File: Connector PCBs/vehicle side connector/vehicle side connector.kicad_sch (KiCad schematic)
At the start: 0 parts

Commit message: added connectors and pinout to schematics, imported board outline
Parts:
- added H? (x3): MountingHole_Pad, symbol Mechanical:MountingHole_Pad
- added J?: Conn_02x04_Odd_Even, symbol Connector_Generic:Conn_02x04_Odd_Even
- added J?: Conn_02x16_Odd_Even, symbol Connector_Generic:Conn_02x16_Odd_Even
- added J?: Conn_02x11_Odd_Even, symbol Connector_Generic:Conn_02x11_Odd_Even
- added J?: Conn_02x10_Odd_Even, symbol Connector_Generic:Conn_02x10_Odd_Even
- added R?: R, symbol Device:R
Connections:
- new net 5V: J?.14 (Pin_14), J?.16 (Pin_16), J?.21 (Pin_21), J?.22 (Pin_22)
- new net 5V_IN: J?.17 (Pin_17)
- new net CAN_H: J?.13 (Pin_13), J?.2 (Pin_2), J?.2 (Pin_2)
- new net CAN_L: J?.15 (Pin_15), J?.4 (Pin_4), J?.4 (Pin_4)
- new net CAPTURE: J?.17 (Pin_17), J?.8 (Pin_8)
- new net C_1: J?.1 (Pin_1)
- new net C_10: J?.10 (Pin_10)
- new net C_11: J?.11 (Pin_11)
- new net C_12: J?.12 (Pin_12)
- new net C_2: J?.2 (Pin_2)
- new net C_3: J?.3 (Pin_3)
- new net C_4: J?.4 (Pin_4)
- new net C_5: J?.5 (Pin_5)
- new net C_6: J?.6 (Pin_6)
- new net C_7: J?.7 (Pin_7)
- new net C_8: J?.8 (Pin_8)
- new net C_9: J?.9 (Pin_9)
- new net Detect: J?.20 (Pin_20), R?.1
- new net ETH_RXN: J?.11 (Pin_11), J?.7 (Pin_7)
- new net ETH_RXP: J?.5 (Pin_5), J?.9 (Pin_9)
- new net ETH_TXN: J?.3 (Pin_3), J?.5 (Pin_5)
- new net ETH_TXP: J?.1 (Pin_1), J?.3 (Pin_3)
- new net GND: H?.1, H?.1, H?.1, J?.1 (Pin_1), J?.13 (Pin_13), J?.18 (Pin_18), J?.18 (Pin_18), J?.2 (Pin_2), J?.20 (Pin_20), J?.22 (Pin_22), J?.23 (Pin_23), J?.24 (Pin_24), J?.29 (Pin_29), J?.4 (Pin_4), J?.6 (Pin_6), J?.7 (Pin_7), J?.8 (Pin_8), R?.2
- new net GPS_PPS: J?.16 (Pin_16), J?.6 (Pin_6)
- new net I2C_SCL: J?.10 (Pin_10), J?.14 (Pin_14), J?.6 (Pin_6)
- new net I2C_SDA: J?.12 (Pin_12), J?.16 (Pin_16), J?.8 (Pin_8)
- new net S_BUS: J?.14 (Pin_14), J?.31 (Pin_31)
- new net TRIG: J?.15 (Pin_15), J?.21 (Pin_21)
- new net UART_RX: J?.12 (Pin_12), J?.27 (Pin_27)
- new net UART_TX: J?.10 (Pin_10), J?.25 (Pin_25)
- new net USB DM: J?.11 (Pin_11), J?.17 (Pin_17)
- new net USB DP: J?.15 (Pin_15), J?.9 (Pin_9)
- new net USB_VBUS: J?.13 (Pin_13), J?.19 (Pin_19)
- new net V_BATT+: J?.1 (Pin_1), J?.26 (Pin_26), J?.28 (Pin_28), J?.3 (Pin_3), J?.30 (Pin_30), J?.32 (Pin_32), J?.5 (Pin_5), J?.7 (Pin_7)
- no-connect marks 0 -> 4
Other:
- note added: "BATT COM Connector"
- note added: "Batt Power Connector"
- note added: "Intermediate Breakout Connector"
- note added: "Payload Connector"

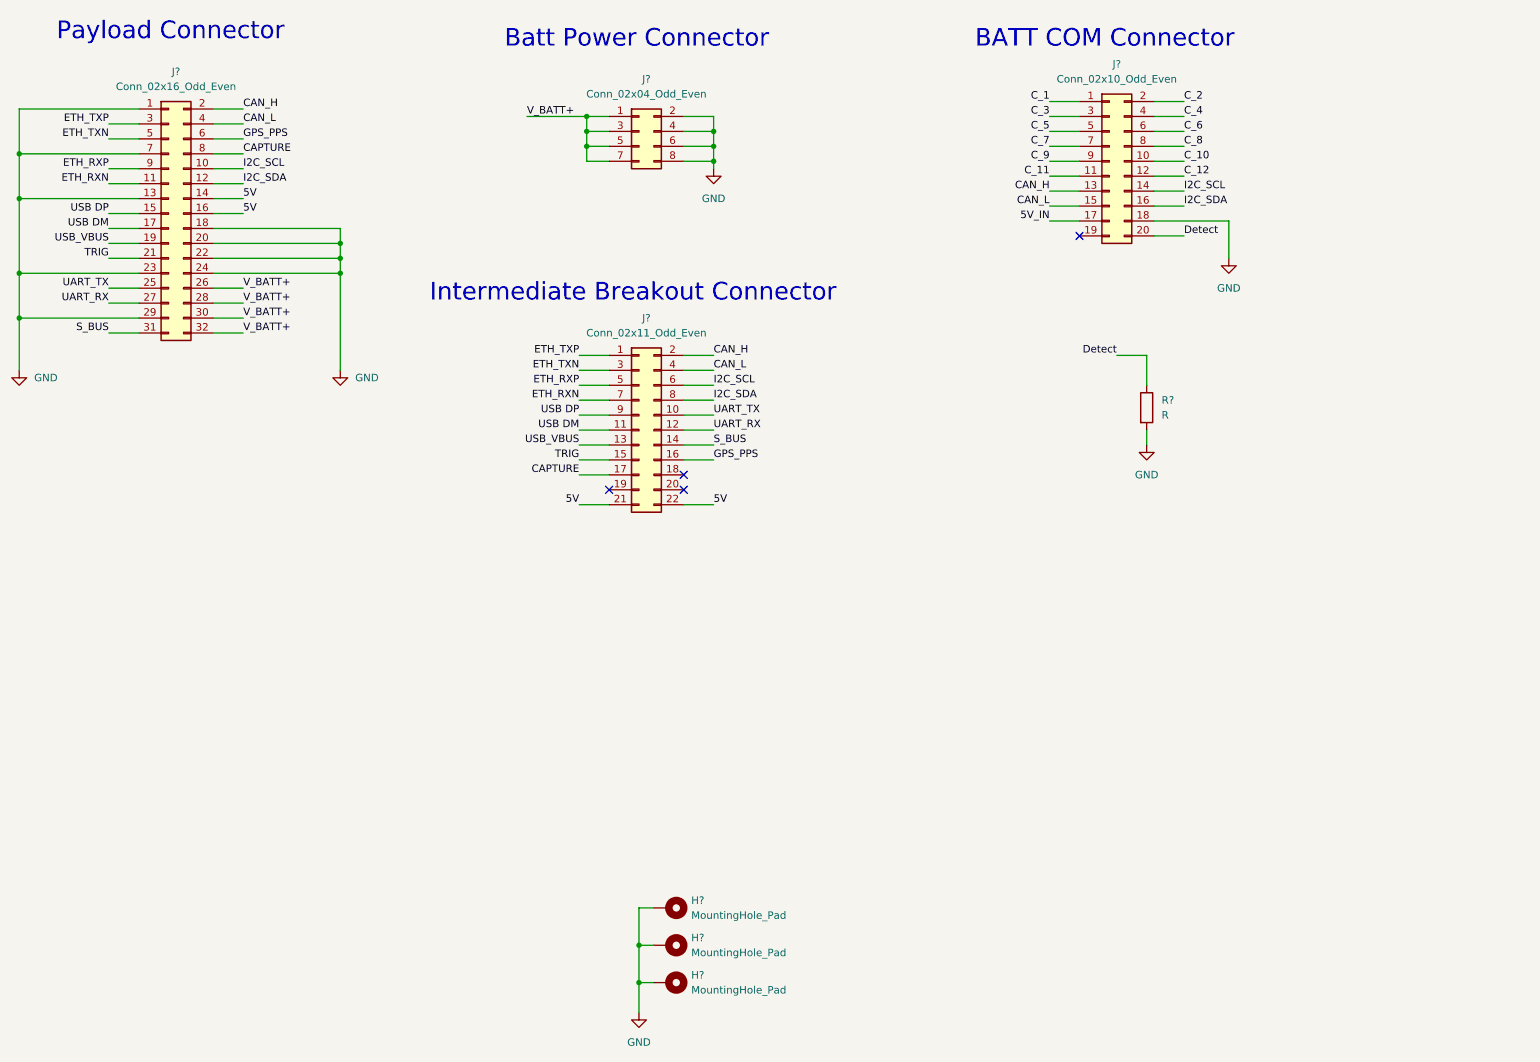
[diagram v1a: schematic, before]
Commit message: added card edge footprints and updated detect pin in schmeatic
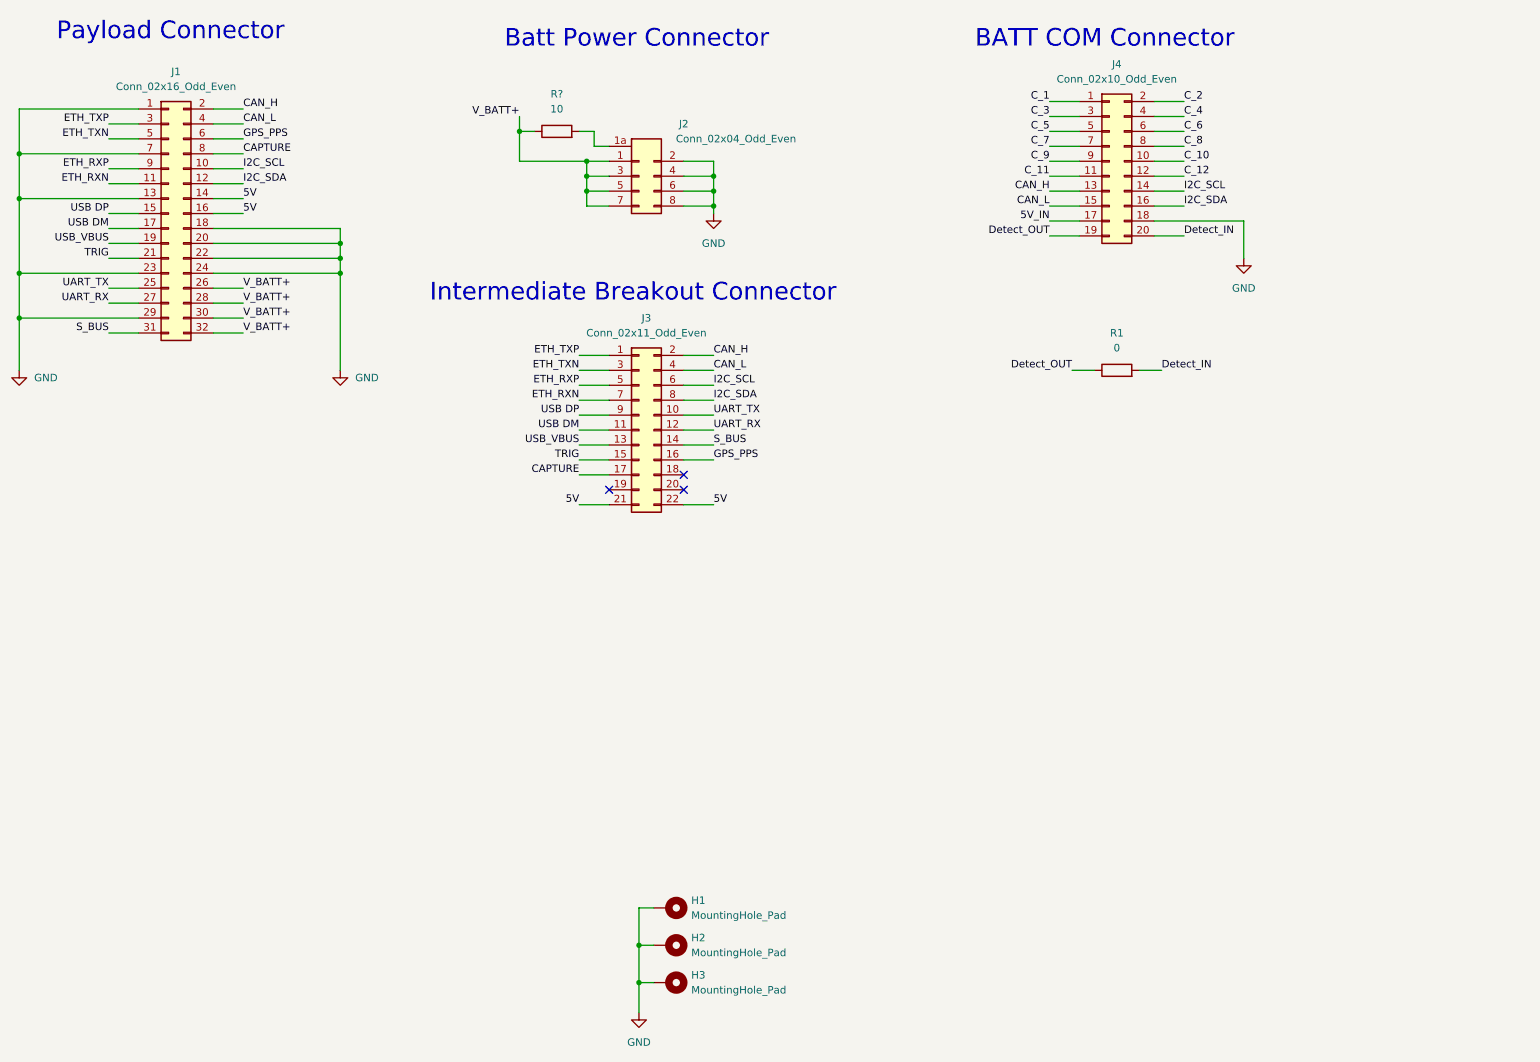
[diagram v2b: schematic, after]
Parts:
- added R?: 10, symbol Device:R
- J1: renamed from J?; footprint (none) -> AERPAW:LPH Signal 32
- J2: renamed from J?; footprint (none) -> AERPAW:LPH Power 8
- J4: renamed from J?; footprint (none) -> AERPAW:LPH Signal 20
- R1: renamed from R?; value R -> 0
- gave numbers to parts that had none: 4
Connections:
- net GND: no longer R1.2
- net V_BATT+: now also R?.1
- net Detect_OUT: now reaches J4.19 (Pin_19)
- net Detect_OUT: now also R1.1
- net Detect renamed Detect_IN
- net Detect_IN: now also R1.2; no longer R1.1
- new net: J2.1a (Pin_1), R?.2
- no-connect marks 4 -> 3
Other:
- moved on the sheet: R1

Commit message: testing why the mechanical stuff isnt added
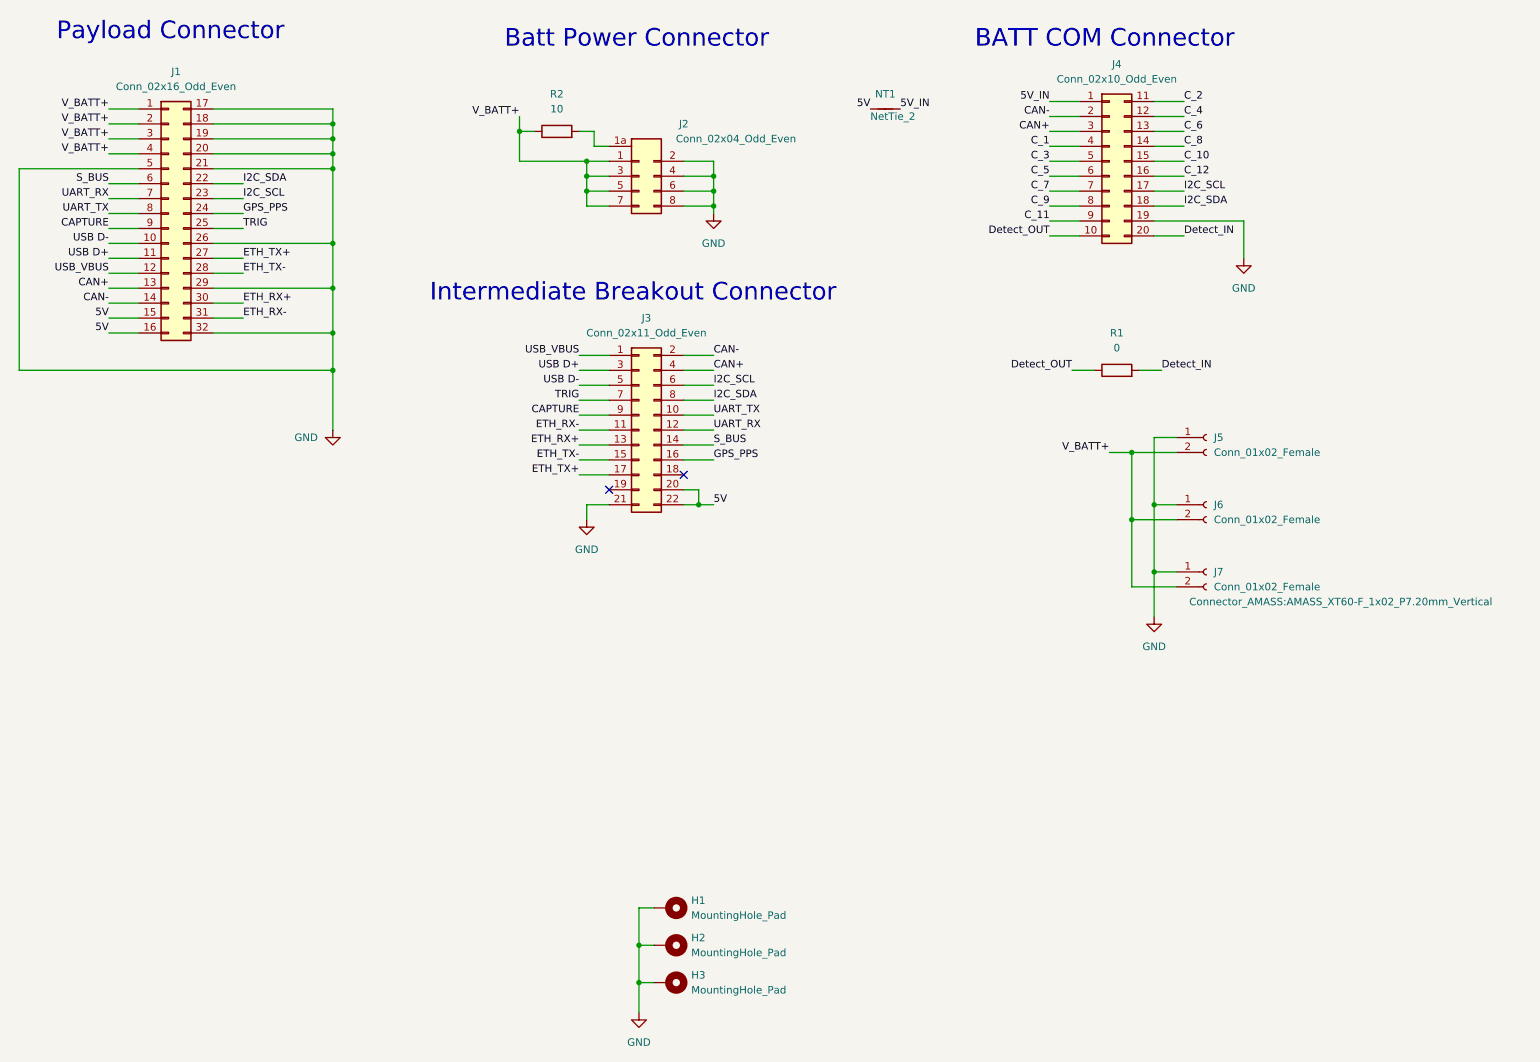
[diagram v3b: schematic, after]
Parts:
- added J5, J7: Conn_01x02_Female, Connector_AMASS:AMASS_XT60-F_1x02_P7.20mm_Vertical, symbol Connector:Conn_01x02_Female
- added J6: Conn_01x02_Female, AERPAW:AMASS_XT90 Vert, symbol Connector:Conn_01x02_Female
- added NT1: NetTie_2, NetTie:NetTie-2_SMD_Pad0.5mm, symbol Device:NetTie_2
- J1: symbol Connector_Generic:Conn_02x16_Odd_Even -> Connector_Generic:Conn_02x16_Top_Bottom
- J3: footprint (none) -> AERPAW:MOLEX_5031542290
- J4: symbol Connector_Generic:Conn_02x10_Odd_Even -> Connector_Generic:Conn_02x10_Top_Bottom
- R1: footprint (none) -> Resistor_SMD:R_1206_3216Metric
- R2: renamed from R?; footprint (none) -> Resistor_SMD:R_2512_6332Metric
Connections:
- net 5V: now also J1.15 (Pin_15), J3.20 (Pin_20), NT1.1; no longer J1.14 (Pin_14), J3.21 (Pin_21)
- net 5V_IN: now also J4.1 (Pin_1), NT1.2; no longer J4.17 (Pin_17)
- net CAPTURE: now also J1.9 (Pin_9), J3.9 (Pin_9); no longer J1.8 (Pin_8), J3.17 (Pin_17)
- net C_1: now also J4.4 (Pin_4); no longer J4.1 (Pin_1)
- net C_10: now also J4.15 (Pin_15); no longer J4.10 (Pin_10)
- net C_11: now also J4.9 (Pin_9); no longer J4.11 (Pin_11)
- net C_12: now also J4.16 (Pin_16); no longer J4.12 (Pin_12)
- net C_2: now also J4.11 (Pin_11); no longer J4.2 (Pin_2)
- net C_3: now also J4.5 (Pin_5); no longer J4.3 (Pin_3)
- net C_4: now also J4.12 (Pin_12); no longer J4.4 (Pin_4)
- net C_5: now also J4.6 (Pin_6); no longer J4.5 (Pin_5)
- net C_6: now also J4.13 (Pin_13); no longer J4.6 (Pin_6)
- net C_8: now also J4.14 (Pin_14); no longer J4.8 (Pin_8)
- net C_9: now also J4.8 (Pin_8); no longer J4.9 (Pin_9)
- net Detect_OUT: now also J4.10 (Pin_10); no longer J4.19 (Pin_19)
- net GND: now also J1.17 (Pin_17), J1.19 (Pin_19), J1.21 (Pin_21), J1.26 (Pin_26), J1.32 (Pin_32), J1.5 (Pin_5), J3.21 (Pin_21), J4.19 (Pin_19), J5.1 (Pin_1), J6.1 (Pin_1), J7.1 (Pin_1); no longer J1.1 (Pin_1), J1.13 (Pin_13), J1.22 (Pin_22), J1.23 (Pin_23), J1.24 (Pin_24), J1.7 (Pin_7), J4.18 (Pin_18)
- net GPS_PPS: now also J1.24 (Pin_24); no longer J1.6 (Pin_6)
- net I2C_SCL: now also J1.23 (Pin_23), J4.17 (Pin_17); no longer J1.10 (Pin_10), J4.14 (Pin_14)
- net I2C_SDA: now also J1.22 (Pin_22), J4.18 (Pin_18); no longer J1.12 (Pin_12), J4.16 (Pin_16)
- net S_BUS: now also J1.6 (Pin_6); no longer J1.31 (Pin_31)
- net TRIG: now also J1.25 (Pin_25), J3.7 (Pin_7); no longer J1.21 (Pin_21), J3.15 (Pin_15)
- net UART_RX: now also J1.7 (Pin_7); no longer J1.27 (Pin_27)
- net UART_TX: now also J1.8 (Pin_8); no longer J1.25 (Pin_25)
- net USB_VBUS: now also J1.12 (Pin_12), J3.1 (Pin_1); no longer J1.19 (Pin_19), J3.13 (Pin_13)
- net V_BATT+: now also J1.1 (Pin_1), J1.2 (Pin_2), J1.3 (Pin_3), J1.4 (Pin_4), J5.2 (Pin_2), J6.2 (Pin_2), J7.2 (Pin_2); no longer J1.26 (Pin_26), J1.28 (Pin_28), J1.30 (Pin_30), J1.32 (Pin_32)
- removed net CAN_H: J1.2 (Pin_2), J3.2 (Pin_2), J4.13 (Pin_13)
- removed net CAN_L: J1.4 (Pin_4), J3.4 (Pin_4), J4.15 (Pin_15)
- net ETH_RXN renamed USB D+
- net USB D+: now also J3.3 (Pin_3); no longer J3.7 (Pin_7)
- net ETH_RXP renamed USB D-
- net USB D-: now also J1.10 (Pin_10); no longer J1.9 (Pin_9)
- removed net ETH_TXN: J1.5 (Pin_5), J3.3 (Pin_3)
- removed net ETH_TXP: J1.3 (Pin_3), J3.1 (Pin_1)
- net USB DM renamed ETH_RX-
- net ETH_RX-: now also J1.31 (Pin_31); no longer J1.17 (Pin_17)
- removed net USB DP: J1.15 (Pin_15), J3.9 (Pin_9)
- new net CAN+: J1.13 (Pin_13), J3.4 (Pin_4), J4.3 (Pin_3)
- new net CAN-: J1.14 (Pin_14), J3.2 (Pin_2), J4.2 (Pin_2)
- new net ETH_RX+: J1.30 (Pin_30), J3.13 (Pin_13)
- new net ETH_TX+: J1.27 (Pin_27), J3.17 (Pin_17)
- new net ETH_TX-: J1.28 (Pin_28), J3.15 (Pin_15)
- no-connect marks 3 -> 2

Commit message: completed drone side connector PCB
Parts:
- removed H1, H2, H3: MountingHole_Pad, symbol Mechanical:MountingHole_Pad
- removed NT1: NetTie_2, NetTie:NetTie-2_SMD_Pad0.5mm, symbol Device:NetTie_2
- added H1, H2, H3: MountingHole, MountingHole:MountingHole_3.2mm_M3, symbol Mechanical:MountingHole
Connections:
- net 5V_IN is gone; now on net 5V: J4.1 (Pin_1)
- net GND: now also J1.12 (Pin_12); no longer J1.32 (Pin_32)
- net USB_VBUS: now also J1.32 (Pin_32); no longer J1.12 (Pin_12)
